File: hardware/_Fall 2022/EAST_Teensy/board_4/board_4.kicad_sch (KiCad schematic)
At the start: 13 parts, among them J1 Conn_01x04, J2 Conn_02x10_Counter_Clockwise, U1 Teensy4.1

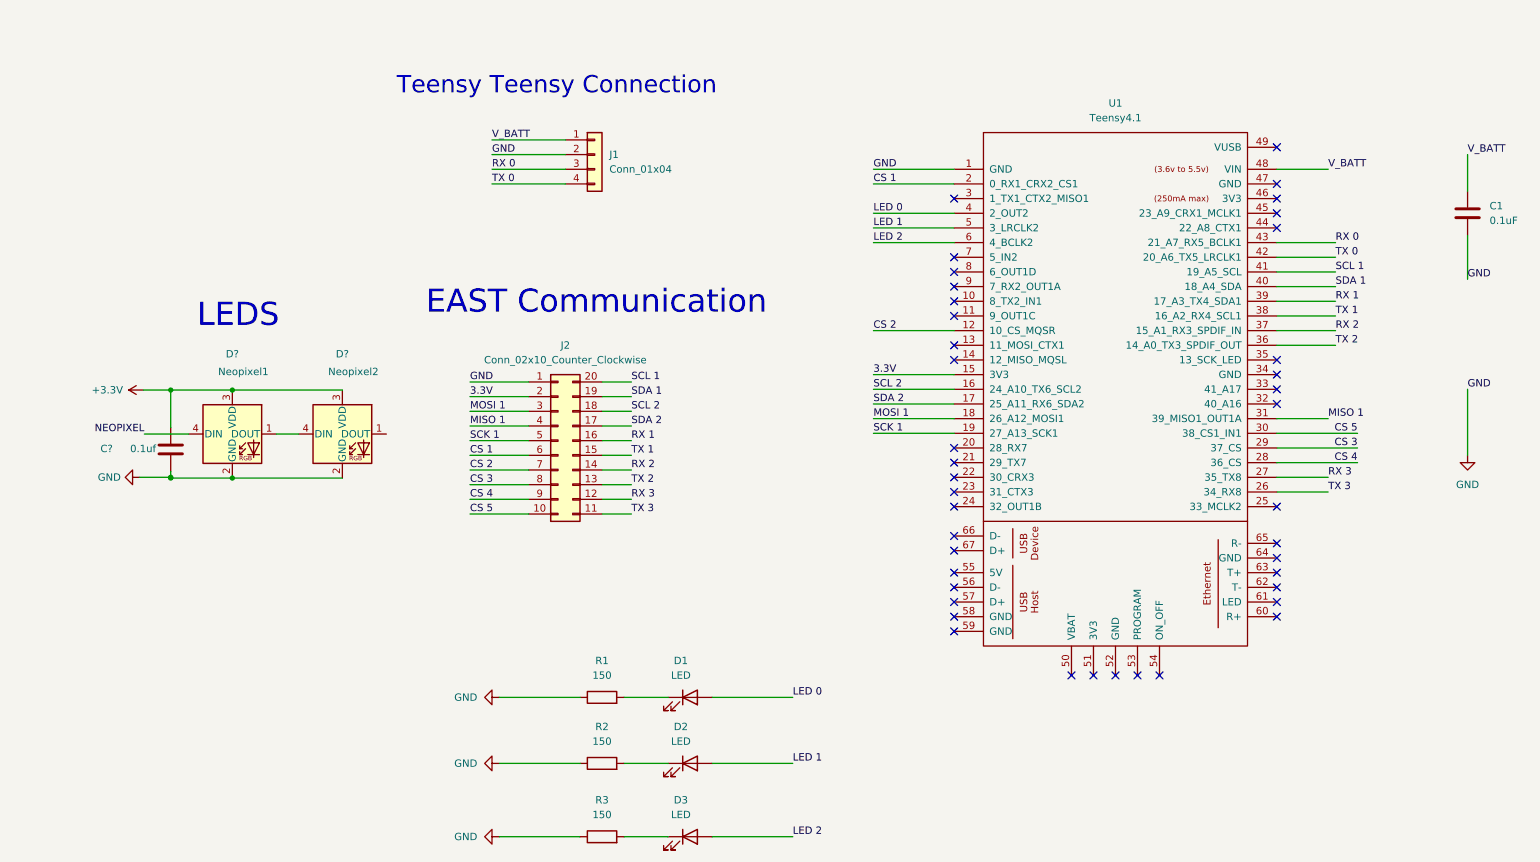
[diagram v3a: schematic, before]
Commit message: Change teensy serial labeling
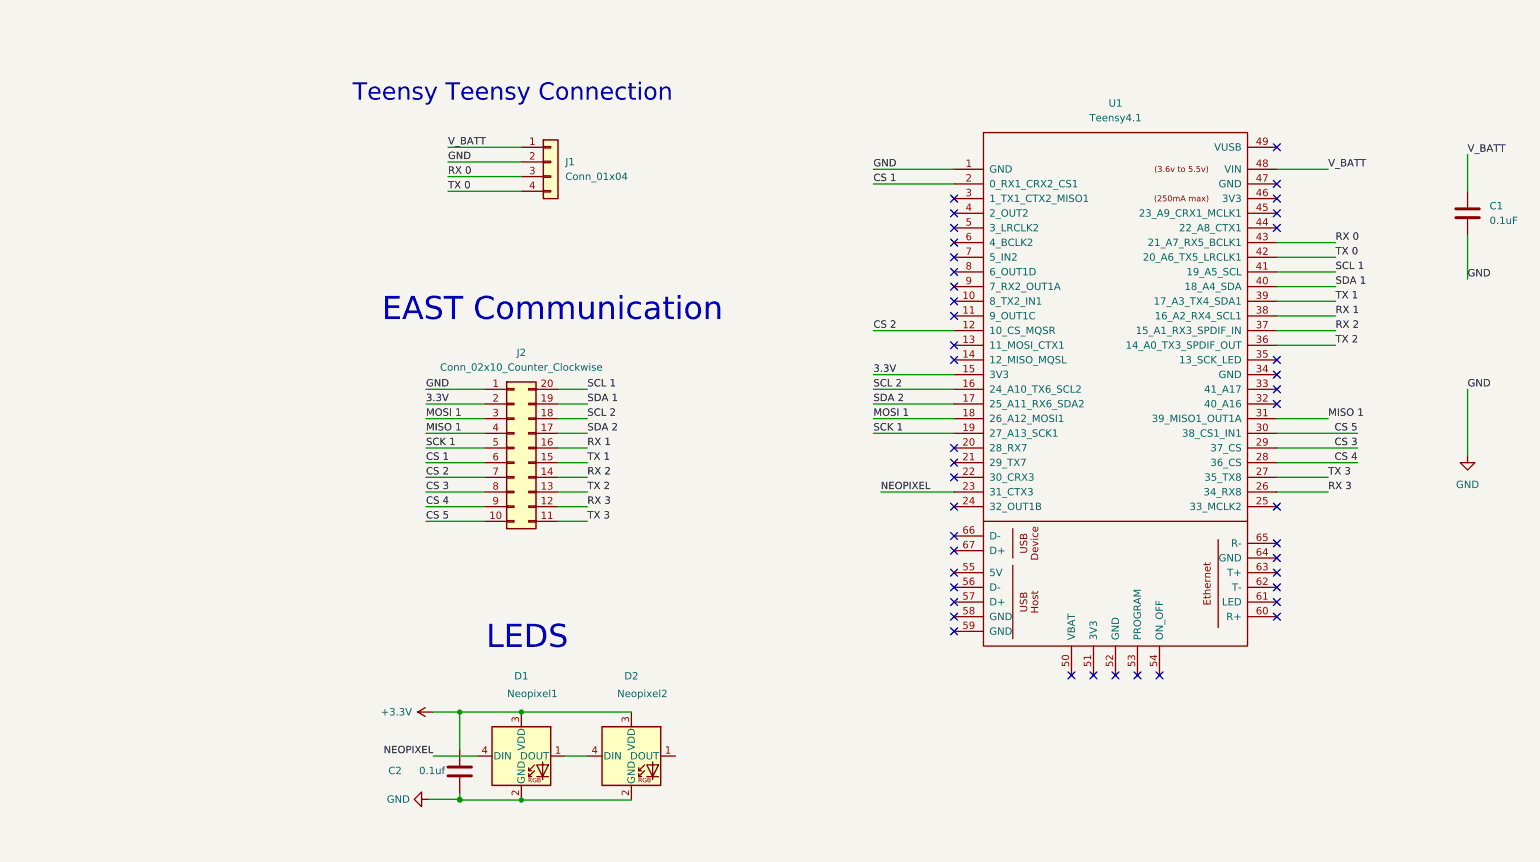
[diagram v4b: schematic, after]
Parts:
- removed D1, D2, D3: LED, LED_SMD:LED_0201_0603Metric, symbol Device:LED
- removed R1, R2, R3: 150, Resistor_SMD:R_0201_0603Metric, symbol Device:R
- gave numbers to parts that had none: 3
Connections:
- net NEOPIXEL: now also U1.23 (31_CTX3)
- net RX 1: now also U1.38 (16_A2_RX4_SCL1); no longer U1.39 (17_A3_TX4_SDA1)
- net RX 3: now also U1.26 (34_RX8); no longer U1.27 (35_TX8)
- net TX 1: now also U1.39 (17_A3_TX4_SDA1); no longer U1.38 (16_A2_RX4_SCL1)
- net TX 3: now also U1.27 (35_TX8); no longer U1.26 (34_RX8)
- net LED 0: no longer names the net of U1.4 (2_OUT2)
- net LED 1: no longer names the net of U1.5 (3_LRCLK2)
- net LED 2: no longer names the net of U1.6 (4_BCLK2)
- no-connect marks 41 -> 43
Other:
- moved on the sheet: C2, D1, D2, J1, J2

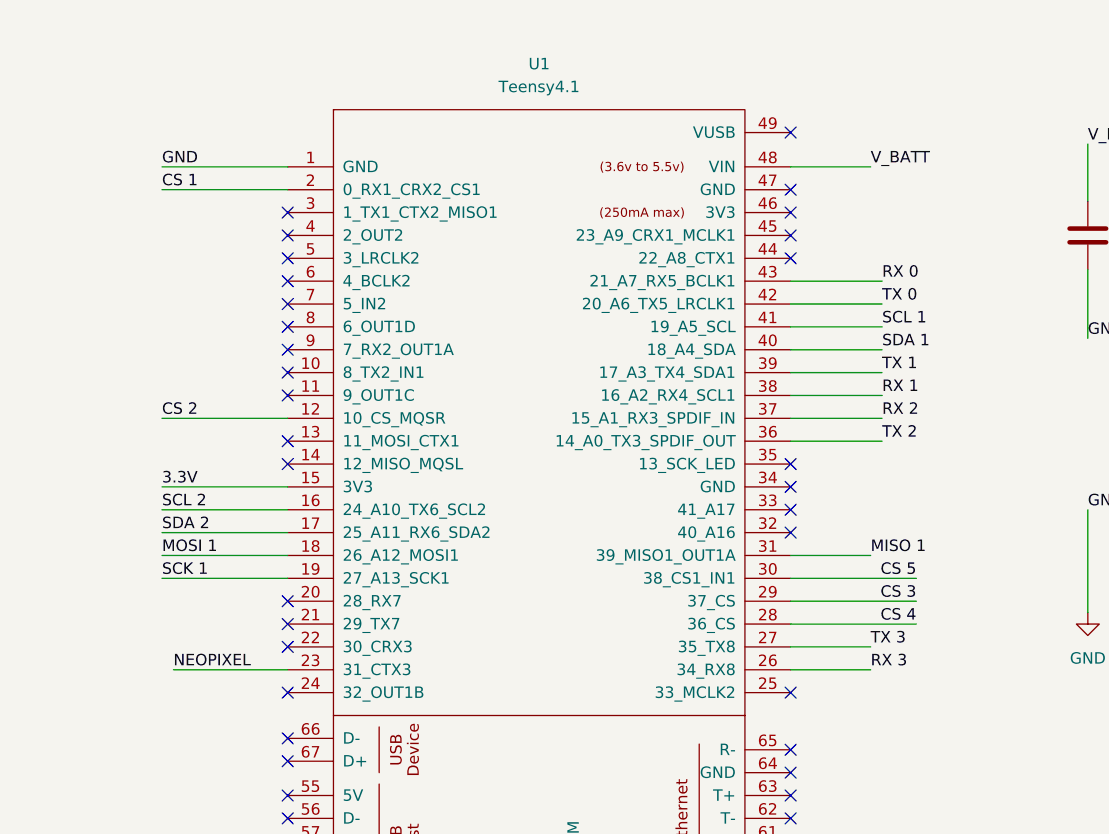
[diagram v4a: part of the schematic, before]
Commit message: Standardize labeling
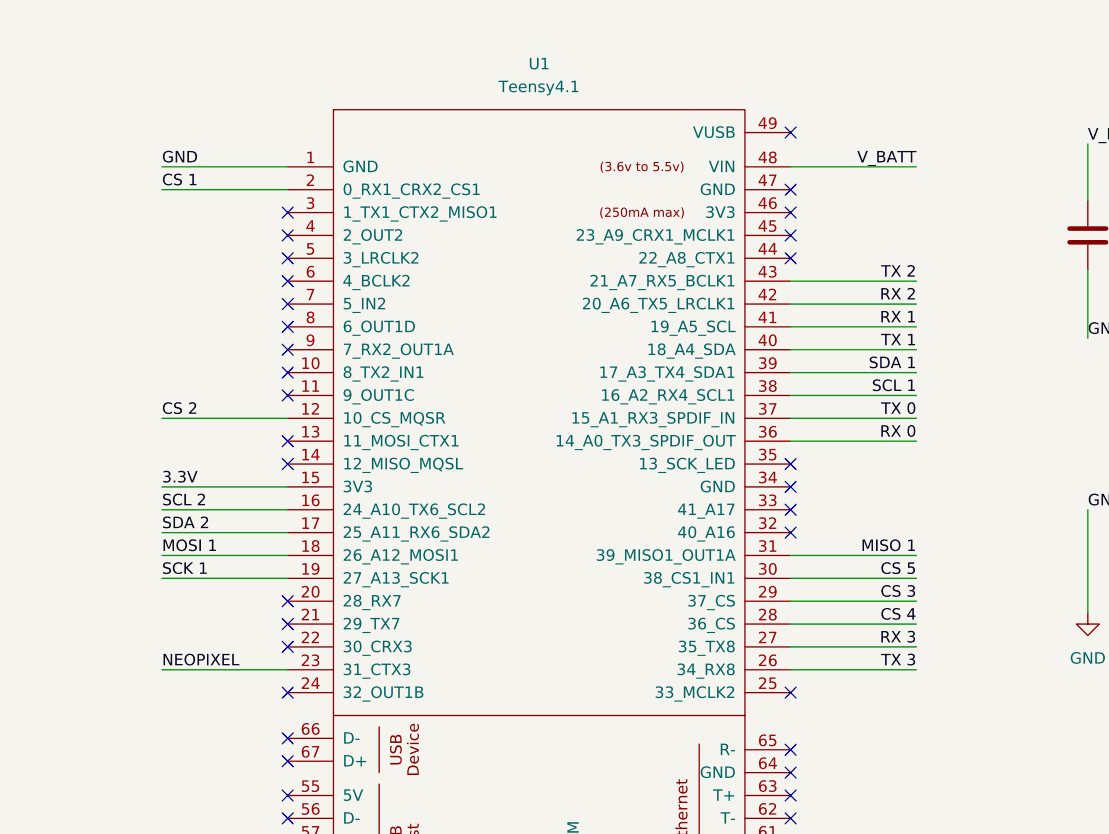
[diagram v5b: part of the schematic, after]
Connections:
- net RX 0: now also U1.36 (14_A0_TX3_SPDIF_OUT); no longer U1.43 (21_A7_RX5_BCLK1)
- net RX 1: now also U1.41 (19_A5_SCL); no longer U1.38 (16_A2_RX4_SCL1)
- net RX 2: now also U1.42 (20_A6_TX5_LRCLK1); no longer U1.37 (15_A1_RX3_SPDIF_IN)
- net RX 3: now also U1.27 (35_TX8); no longer U1.26 (34_RX8)
- net SCL 1: now also U1.38 (16_A2_RX4_SCL1); no longer U1.41 (19_A5_SCL)
- net SDA 1: now also U1.39 (17_A3_TX4_SDA1); no longer U1.40 (18_A4_SDA)
- net TX 0: now also U1.37 (15_A1_RX3_SPDIF_IN); no longer U1.42 (20_A6_TX5_LRCLK1)
- net TX 1: now also U1.40 (18_A4_SDA); no longer U1.39 (17_A3_TX4_SDA1)
- net TX 2: now also U1.43 (21_A7_RX5_BCLK1); no longer U1.36 (14_A0_TX3_SPDIF_OUT)
- net TX 3: now also U1.26 (34_RX8); no longer U1.27 (35_TX8)
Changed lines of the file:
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@@
     (stroke (width 0) (type default) (color 0 0 0 0))
   )
-  (wire (pts (xy 231.14 39.37) (xy 240.03 39.37))
+  (wire (pts (xy 231.14 39.37) (xy 245.11 39.37))
     (stroke (width 0) (type default) (color 0 0 0 0))
   )
@@
     (stroke (width 0) (type default) (color 0 0 0 0))
   )
-  (wire (pts (xy 231.14 59.69) (xy 241.3 59.69))
+  (wire (pts (xy 231.14 59.69) (xy 245.11 59.69))
     (stroke (width 0) (type default) (color 0 0 0 0))
   )
@@
     (stroke (width 0) (type default) (color 0 0 0 0))
   )
-  (wire (pts (xy 231.14 82.55) (xy 240.03 82.55))
+  (wire (pts (xy 231.14 82.55) (xy 245.11 82.55))
     (stroke (width 0) (type default) (color 0 0 0 0))
   )
@@
     (stroke (width 0) (type default) (color 0 0 0 0))
   )
-  (wire (pts (xy 231.14 62.23) (xy 241.3 62.23))
+  (wire (pts (xy 231.14 62.23) (xy 245.11 62.23))
     (stroke (width 0) (type default) (color 0 0 0 0))
   )
@@
     (stroke (width 0) (type default) (color 0 0 0 0))
   )
-  (wire (pts (xy 231.14 57.15) (xy 241.3 57.15))
+  (wire (pts (xy 231.14 57.15) (xy 245.11 57.15))
     (stroke (width 0) (type default) (color 0 0 0 0))
   )
@@
     (stroke (width 0) (type default) (color 0 0 0 0))
   )
-  (wire (pts (xy 231.14 67.31) (xy 241.3 67.31))
-    (stroke (width 0) (type default) (color 0 0 0 0))
-  )
-  (wire (pts (xy 231.14 64.77) (xy 241.3 64.77))
+  (wire (pts (xy 231.14 67.31) (xy 245.11 67.31))
+    (stroke (width 0) (type default) (color 0 0 0 0))
+  )
+  (wire (pts (xy 231.14 64.77) (xy 245.11 64.77))
     (stroke (width 0) (type default) (color 0 0 0 0))
   )
@@
     (stroke (width 0) (type default) (color 0 0 0 0))
   )
-  (wire (pts (xy 231.14 54.61) (xy 241.3 54.61))
+  (wire (pts (xy 231.14 54.61) (xy 245.11 54.61))
     (stroke (width 0) (type default) (color 0 0 0 0))
   )
@@
     (stroke (width 0) (type default) (color 0 0 0 0))
   )
-  (wire (pts (xy 231.14 69.85) (xy 241.3 69.85))
-    (stroke (width 0) (type default) (color 0 0 0 0))
-  )
-  (wire (pts (xy 231.14 92.71) (xy 240.03 92.71))
+  (wire (pts (xy 231.14 69.85) (xy 245.11 69.85))
+    (stroke (width 0) (type default) (color 0 0 0 0))
+  )
+  (wire (pts (xy 231.14 92.71) (xy 245.11 92.71))
     (stroke (width 0) (type default) (color 0 0 0 0))
   )
@@
     (stroke (width 0) (type default) (color 0 0 0 0))
   )
-  (wire (pts (xy 231.14 52.07) (xy 241.3 52.07))
+  (wire (pts (xy 231.14 52.07) (xy 245.11 52.07))
     (stroke (width 0) (type default) (color 0 0 0 0))
   )
@@
     (stroke (width 0) (type default) (color 0 0 0 0))
   )
-  (wire (pts (xy 162.56 95.25) (xy 175.26 95.25))
+  (wire (pts (xy 161.29 95.25) (xy 175.26 95.25))
     (stroke (width 0) (type default) (color 0 0 0 0))
   )
@@
     (stroke (width 0) (type default) (color 0 0 0 0))
   )
-  (wire (pts (xy 231.14 95.25) (xy 240.03 95.25))
+  (wire (pts (xy 231.14 95.25) (xy 245.11 95.25))
     (stroke (width 0) (type default) (color 0 0 0 0))
   )
@@
     (effects (font (size 1.27 1.27)) (justify left bottom))
   )
-  (label "RX 2" (at 241.3 67.31 0)
-    (effects (font (size 1.27 1.27)) (justify left bottom))
+  (label "RX 2" (at 245.11 54.61 180)
+    (effects (font (size 1.27 1.27)) (justify right bottom))
   )
   (label "MISO 1" (at 83.82 85.09 0)
     (effects (font (size 1.27 1.27)) (justify left bottom))
   )
-  (label "RX 1" (at 241.3 64.77 0)
-    (effects (font (size 1.27 1.27)) (justify left bottom))
+  (label "RX 1" (at 245.11 57.15 180)
+    (effects (font (size 1.27 1.27)) (justify right bottom))
   )
   (label "MOSI 1" (at 83.82 82.55 0)
     (effects (font (size 1.27 1.27)) (justify left bottom))
   )
-  (label "TX 2" (at 241.3 69.85 0)
-    (effects (font (size 1.27 1.27)) (justify left bottom))
+  (label "TX 2" (at 245.11 52.07 180)
+    (effects (font (size 1.27 1.27)) (justify right bottom))
   )
   (label "RX 0" (at 87.63 40.64 0)
@@
     (effects (font (size 1.27 1.27)) (justify left bottom))
   )
-  (label "RX 0" (at 241.3 52.07 0)
-    (effects (font (size 1.27 1.27)) (justify left bottom))
+  (label "RX 0" (at 245.11 69.85 180)
+    (effects (font (size 1.27 1.27)) (justify right bottom))
   )
   (label "CS 1" (at 161.29 41.91 0)
@@
     (effects (font (size 1.27 1.27)) (justify left bottom))
   )
-  (label "TX 0" (at 241.3 54.61 0)
-    (effects (font (size 1.27 1.27)) (justify left bottom))
+  (label "TX 0" (at 245.11 67.31 180)
+    (effects (font (size 1.27 1.27)) (justify right bottom))
   )
   (label "SCK 1" (at 83.82 87.63 0)
@@
     (effects (font (size 1.27 1.27)) (justify right bottom))
   )
-  (label "MISO 1" (at 240.03 82.55 0)
-    (effects (font (size 1.27 1.27)) (justify left bottom))
+  (label "MISO 1" (at 245.11 82.55 180)
+    (effects (font (size 1.27 1.27)) (justify right bottom))
   )
   (label "CS 5" (at 83.82 100.33 0)
@@
     (effects (font (size 1.27 1.27)) (justify left bottom))
   )
-  (label "NEOPIXEL" (at 162.56 95.25 0)
+  (label "NEOPIXEL" (at 161.29 95.25 0)
     (effects (font (size 1.27 1.27)) (justify left bottom))
   )
@@
     (effects (font (size 1.27 1.27)) (justify left bottom))
   )
-  (label "SDA 1" (at 241.3 59.69 0)
-    (effects (font (size 1.27 1.27)) (justify left bottom))
+  (label "SDA 1" (at 245.11 62.23 180)
+    (effects (font (size 1.27 1.27)) (justify right bottom))
   )
   (label "CS 1" (at 83.82 90.17 0)
@@
     (effects (font (size 1.27 1.27)) (justify left bottom))
   )
-  (label "TX 1" (at 241.3 62.23 0)
-    (effects (font (size 1.27 1.27)) (justify left bottom))
-  )
-  (label "V_BATT" (at 240.03 39.37 0)
-    (effects (font (size 1.27 1.27)) (justify left bottom))
+  (label "TX 1" (at 245.11 59.69 180)
+    (effects (font (size 1.27 1.27)) (justify right bottom))
+  )
+  (label "V_BATT" (at 245.11 39.37 180)
+    (effects (font (size 1.27 1.27)) (justify right bottom))
   )
   (label "SCL 2" (at 111.76 82.55 0)
@@
     (effects (font (size 1.27 1.27)) (justify left bottom))
   )
-  (label "SCL 1" (at 241.3 57.15 0)
-    (effects (font (size 1.27 1.27)) (justify left bottom))
+  (label "SCL 1" (at 245.11 64.77 180)
+    (effects (font (size 1.27 1.27)) (justify right bottom))
   )
   (label "CS 3" (at 245.11 87.63 180)
@@
     (effects (font (size 1.27 1.27)) (justify left bottom))
   )
-  (label "TX 3" (at 240.03 92.71 0)
-    (effects (font (size 1.27 1.27)) (justify left bottom))
+  (label "TX 3" (at 245.11 95.25 180)
+    (effects (font (size 1.27 1.27)) (justify right bottom))
   )
   (label "GND" (at 161.29 39.37 0)
@@
     (effects (font (size 1.27 1.27)) (justify left bottom))
   )
-  (label "RX 3" (at 240.03 95.25 0)
-    (effects (font (size 1.27 1.27)) (justify left bottom))
+  (label "RX 3" (at 245.11 92.71 180)
+    (effects (font (size 1.27 1.27)) (justify right bottom))
   )
   (label "SDA 1" (at 111.76 80.01 0)
